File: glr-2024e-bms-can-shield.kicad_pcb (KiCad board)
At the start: 2 copper layers, 70 x 81 mm, 13 parts, among them CN10 Conn_02x19_Odd_Even_MountingP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, CN7 Conn_02x19_Odd_Even_MountingP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, IC1 TLE6250GV33XUMA1, IC2 L9615D013TR, J1 Screw_Terminal_01x08

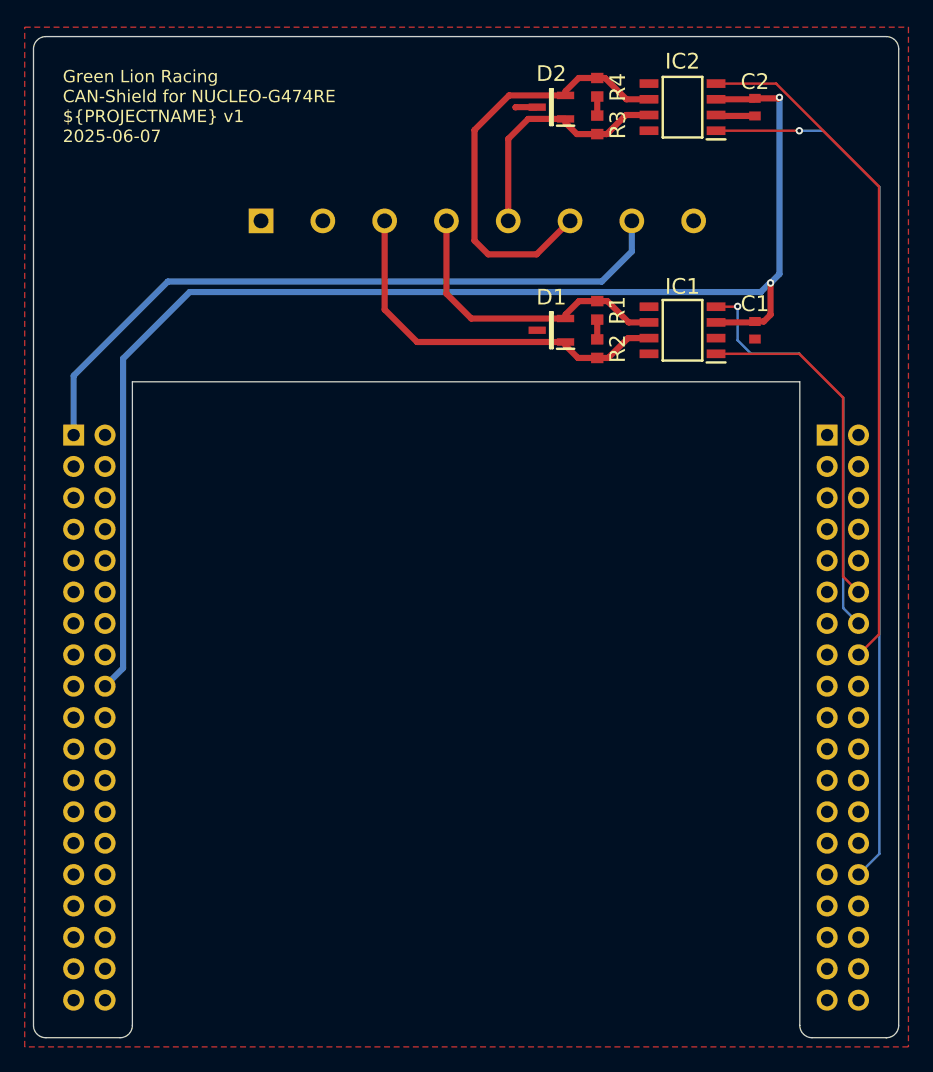
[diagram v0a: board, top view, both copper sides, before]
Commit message: the last touch
I added two transistors. The first one replaces the optocoupler and controls the relay: when 3.3 V is present at the input (which indicates a fault), the transistor switches on and activates the relay. If no voltage is present, the relay remains off.

The second transistor is used to turn the charger on and off. For this purpose, it was necessary to connect 12 V to its collector.
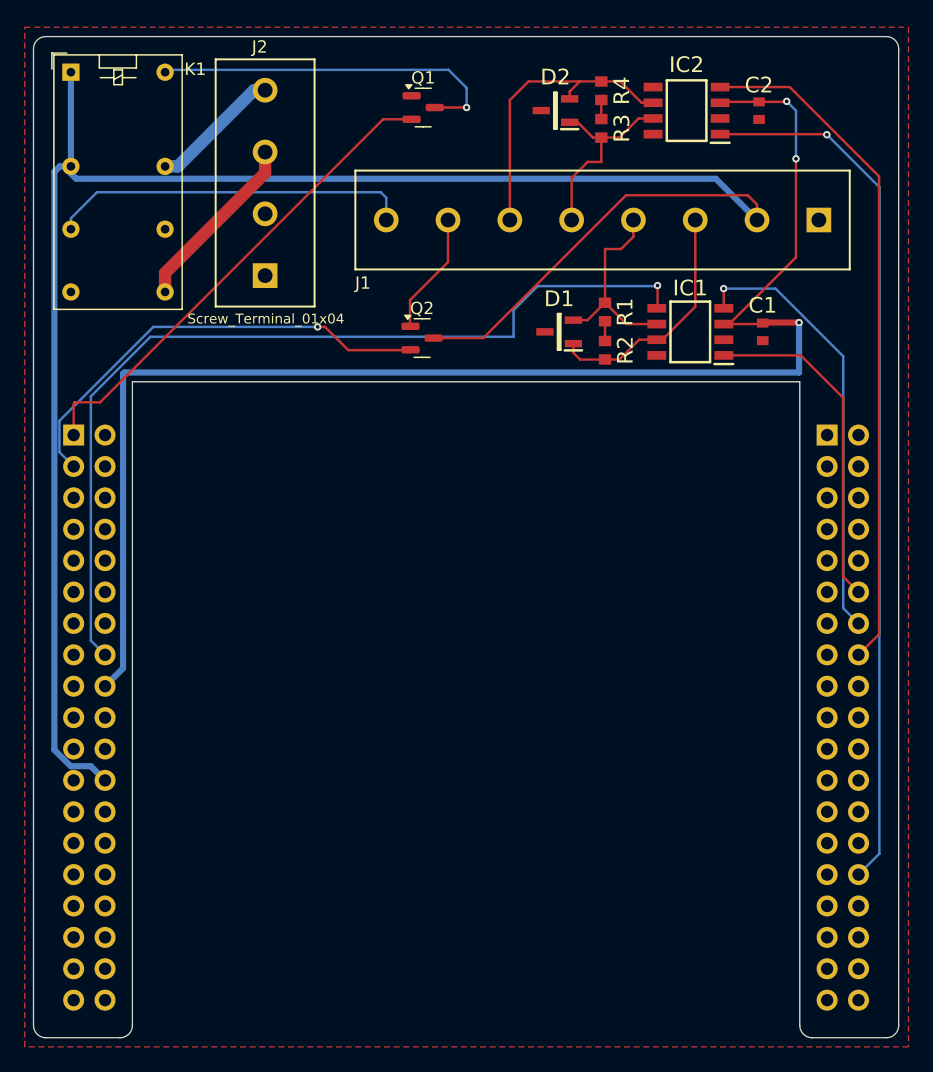
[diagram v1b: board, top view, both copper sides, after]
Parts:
- added J2: Screw_Terminal_01x04, GLR_KiCAD_Library:WECO-950-FB-04, F.Cu at (112.5, 69.6)
- added K1: G5V-2, Relay_THT:Relay_DPDT_Omron_G5V-2, F.Cu at (97.2, 70.6)
- added Q1: BC107, Package_TO_SOT_SMD:SOT-23, F.Cu at (125.7, 73.5)
- added Q2: BC107, Package_TO_SOT_SMD:SOT-23, F.Cu at (125.7, 92.2)
- J1: moved to F.Cu
- moved J1 50.1 mm to (160.2, 82.2), turned to 180 degrees
- moved C1 0.64 mm to (153.2, 91.7)
- moved D1 0.64 mm to (136.7, 91.7)
- moved IC1 0.64 mm to (147.3, 91.7)
- moved R1 0.64 mm to (140.4, 90.0)
- moved R2 0.64 mm to (140.4, 93.1)
- moved IC2 0.43 mm to (147.1, 73.8)
- moved R3 0.43 mm to (140.2, 75.2)
- moved R4 0.43 mm to (140.2, 72.1)
- moved C2 0.43 mm to (152.9, 73.8)
- moved D2 0.43 mm to (136.4, 73.8)
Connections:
- CN7 pad 24: unconnected-(CN7-Pin_24-Pad24) -> +12V
- CN7 pad 3: unconnected-(CN7-Pin_3-Pad3) -> Net-(CN7-Pin_3)
- IC1 pad 5: unconnected-(IC1-V33V-Pad5) -> +3V3
- J1 pad 7: Net-(CN7-Pin_1) -> Net-(J1-Pin_7)
- J1 pad 8: unconnected-(J1-Pin_8-Pad8) -> Net-(J1-Pin_8)
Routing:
- net +12V: track 0.00 -> 151.2 mm
- net +3V3: track 0.00 -> 74.1 mm, vias 0 -> 1
- net Net-(CN7-Pin_3): track 0.00 -> 36.5 mm, vias 0 -> 1
- net Net-(J1-Pin_8): track 0.00 -> 29.3 mm
- net Net-(Q1-C): track 0.00 -> 29.2 mm, vias 0 -> 1
- net Net-(CN7-Pin_1): track 56.6 -> 39.5 mm
- net Net-(J2-Pin_3): track 0.00 -> 14.7 mm
- net /CAN 1 H: track 31.0 -> 19.6 mm
- net /CAN 2 L: track 35.0 -> 24.4 mm
- net Net-(J2-Pin_4): track 0.00 -> 10.6 mm
- net Net-(J1-Pin_7): track 0.00 -> 9.91 mm
- net /CAN 1 L: track 24.6 -> 16.5 mm
- net +5V: track 109.8 -> 117.2 mm, vias 2 -> 3
- net GND: track 5.10 -> 0.00 mm
- net /CAN 2 H: track 20.0 -> 16.2 mm
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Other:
- board text removed: "12V"
- board text removed: "GND"

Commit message: use Würth Elektronik TBL connectors
do some restructuring
add project specific libraries
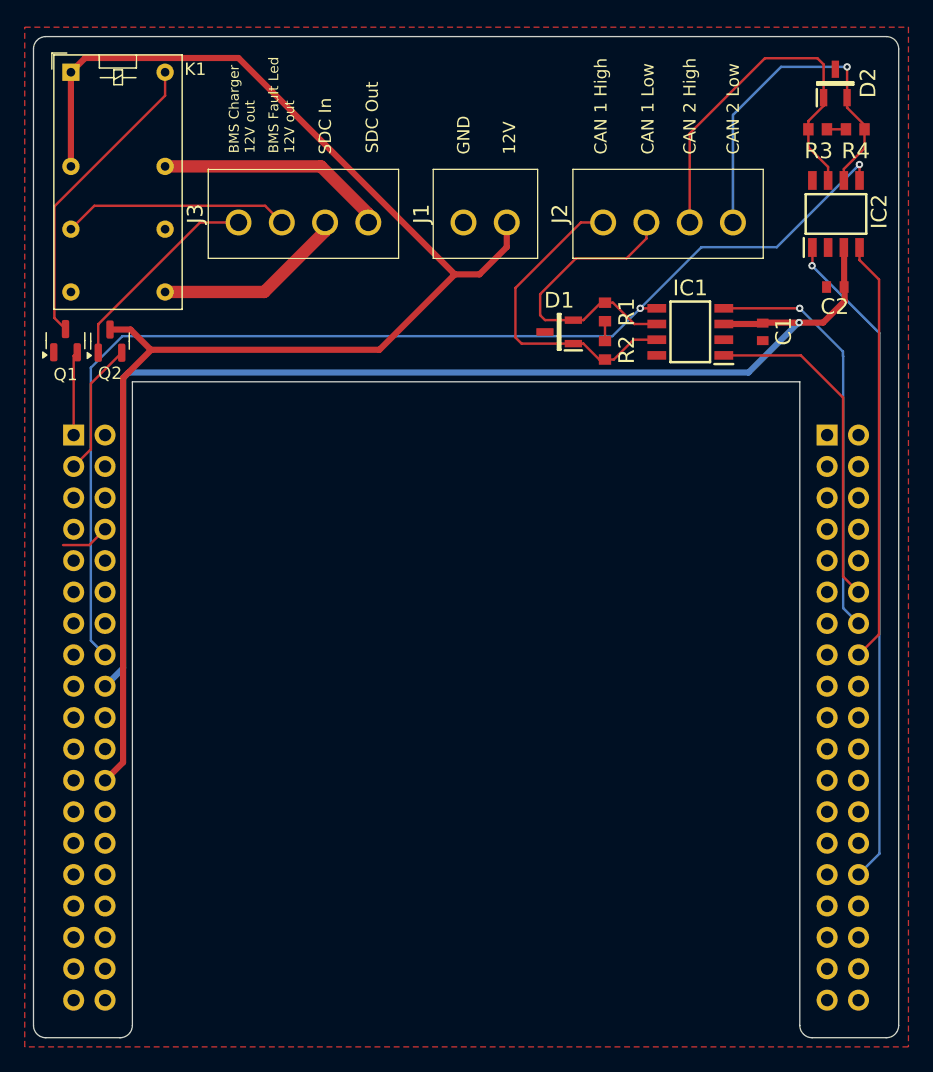
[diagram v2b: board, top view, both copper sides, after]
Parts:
- added J3: 691321100004, SamacSys_Parts:691321100004, F.Cu at (110.8, 82.9)
- IC2: value L9615D013TR -> TLE6250GV33XUMA1
- J1: value Screw_Terminal_01x08 -> 691321100002; footprint GLR_KiCad_Library:WECO-950-FB-08 -> SamacSys_Parts:691321100002
- J2: value Screw_Terminal_01x04 -> 691321100004; footprint GLR_KiCAD_Library:WECO-950-FB-04 -> SamacSys_Parts:691321100004
- moved Q1 34.5 mm to (96.8, 92.4), turned to 90 degrees
- moved J1 31.3 mm to (129.0, 82.9), turned to 0 degrees
- moved J2 30.8 mm to (140.3, 82.9)
- moved Q2 25.3 mm to (100.4, 92.4), turned to 90 degrees
- moved D2 22.8 mm to (159.1, 71.6), turned to 90 degrees
- moved R4 20.8 mm to (160.7, 75.3), turned to 180 degrees
- moved R3 17.5 mm to (157.7, 75.3), turned to 180 degrees
- moved C2 15.6 mm to (159.1, 88.0), turned to 180 degrees
- moved IC2 14.7 mm to (159.1, 82.1), turned to 90 degrees
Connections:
- net Net-(CN7-Pin_1) renamed /BMS_FAULT
- net Net-(CN7-Pin_3) renamed /BMS_CHARGER
- IC2 pad 5: unconnected-(IC2-RX1-Pad5) -> +3V3
- J2 pad 1: unconnected-(J2-Pin_1-Pad1) -> /CAN 1 H
- J2 pad 2: unconnected-(J2-Pin_2-Pad2) -> /CAN 1 L
- J2 pad 3: Net-(J2-Pin_3) -> /CAN 2 H
- J2 pad 4: Net-(J2-Pin_4) -> /CAN 2 L
- K1 pad 13: Net-(J2-Pin_4) -> /SDC_OUT
- K1 pad 6: Net-(J1-Pin_8) -> /BMS_FAULT_LED
- K1 pad 9: Net-(J2-Pin_3) -> /SDC_IN
- Q2 pad 1: Net-(J1-Pin_7) -> /BMS_CHARGER_OUT
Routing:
- net /BMS_FAULT: track 39.5 -> 6.82 mm
- net +12V: track 151.2 -> 121.0 mm
- net Net-(J1-Pin_8): track 29.3 -> 0.00 mm
- net /BMS_CHARGER: track 36.5 -> 10.8 mm, vias 1 -> 0
- net +3V3: track 74.1 -> 95.3 mm, vias 1 -> 2
- net Net-(CN10-Pin_16): track 55.2 -> 34.3 mm
- net +5V: track 117.2 -> 97.0 mm, vias 3 -> 1
- net /SDC_OUT: track 0.00 -> 18.7 mm
- net /BMS_FAULT_LED: track 0.00 -> 18.4 mm
- net Net-(CN10-Pin_30): track 71.0 -> 53.7 mm
- net /BMS_CHARGER_OUT: track 0.00 -> 17.1 mm
- net /SDC_IN: track 0.00 -> 15.7 mm
- net /CAN 2 H: track 16.2 -> 31.3 mm
- net Net-(J2-Pin_3): track 14.7 -> 0.00 mm
- net Net-(J2-Pin_4): track 10.6 -> 0.00 mm
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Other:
- board text added: "12V"
- board text added: "BMS Charger 12V out"
- board text added: "BMS Fault Led 12V out"
- board text added: "GND"
- board text added: "SDC In"
- board text added: "SDC Out"
- board text removed: "AMS Fault"
